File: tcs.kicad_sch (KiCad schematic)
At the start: 7 parts

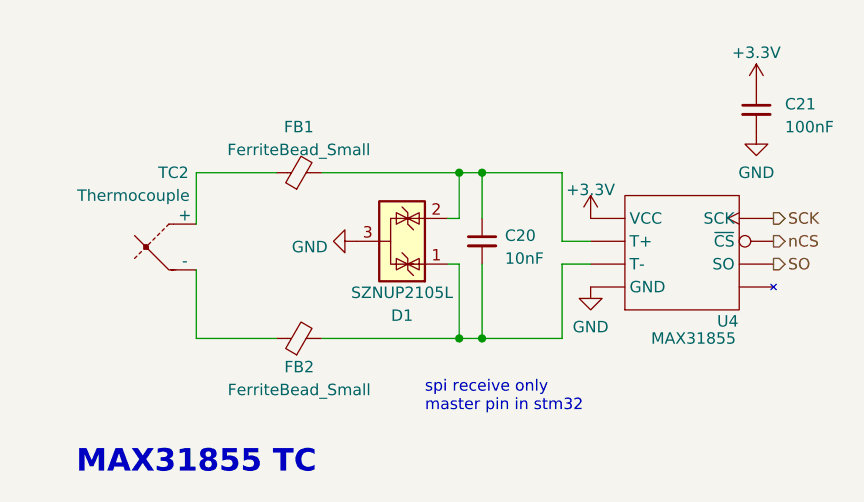
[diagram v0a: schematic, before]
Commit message: fixed resistor values
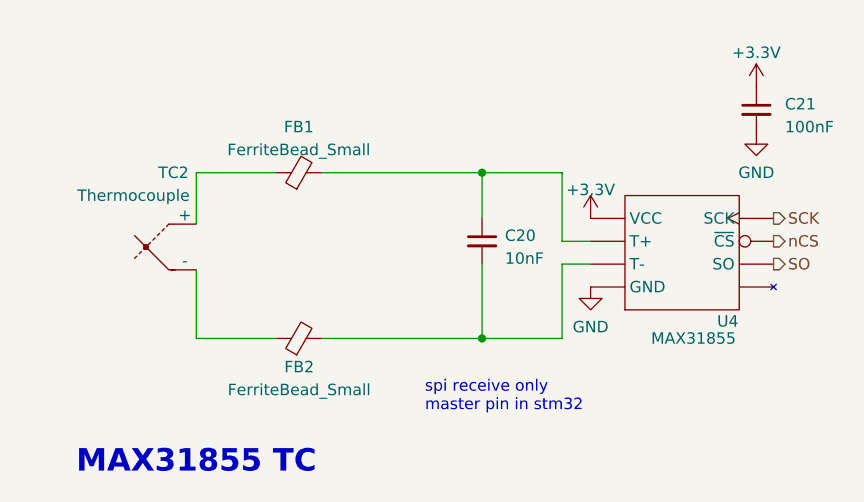
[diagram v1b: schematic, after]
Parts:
- removed D1: SZNUP2105L, Package_TO_SOT_SMD:SOT-23, symbol Power_Protection:SZNUP2105L
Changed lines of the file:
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@@
   (junction (at 143.51 92.075) (diameter 0) (color 0 0 0 0)
   )
-  (junction (at 140.97 73.66) (diameter 0) (color 0 0 0 0)
-  )
   (junction (at 143.51 73.66) (diameter 0) (color 0 0 0 0)
   )
-  (junction (at 140.97 92.075) (diameter 0) (color 0 0 0 0)
-  )
   (wire (pts (xy 111.76 79.375) (xy 111.76 73.66))
     (stroke (width 0) (type default))
@@
     (stroke (width 0) (type default))
   )
-  (wire (pts (xy 139.7 83.82) (xy 140.97 83.82))
-    (stroke (width 0) (type default))
-  )
   (wire (pts (xy 111.76 73.66) (xy 120.65 73.66))
     (stroke (width 0) (type default))
@@
     (stroke (width 0) (type default))
   )
-  (wire (pts (xy 140.97 78.74) (xy 139.7 78.74))
-    (stroke (width 0) (type default))
-  )
-  (wire (pts (xy 125.73 73.66) (xy 140.97 73.66))
+  (wire (pts (xy 125.73 73.66) (xy 143.51 73.66))
     (stroke (width 0) (type default))
   )
@@
     (stroke (width 0) (type default))
   )
-  (wire (pts (xy 125.73 92.075) (xy 140.97 92.075))
-    (stroke (width 0) (type default))
-  )
   (wire (pts (xy 143.51 92.075) (xy 152.4 92.075))
     (stroke (width 0) (type default))
   )
-  (wire (pts (xy 140.97 73.66) (xy 140.97 78.74))
-    (stroke (width 0) (type default))
-  )
-  (wire (pts (xy 140.97 83.82) (xy 140.97 92.075))
-    (stroke (width 0) (type default))
-  )
   (wire (pts (xy 143.51 73.66) (xy 152.4 73.66))
     (stroke (width 0) (type default))
   )
-  (wire (pts (xy 140.97 73.66) (xy 143.51 73.66))
-    (stroke (width 0) (type default))
-  )
   (wire (pts (xy 152.4 81.28) (xy 152.4 73.66))
     (stroke (width 0) (type default))
   )
-  (wire (pts (xy 140.97 92.075) (xy 143.51 92.075))
+  (wire (pts (xy 125.73 92.075) (xy 143.51 92.075))
     (stroke (width 0) (type default))
   )
@@
     )
   )
-  (symbol (lib_id "power:GND") (at 129.54 81.28 270) (unit 1)
-    (in_bom yes) (on_board yes) (dnp no) (fields_autoplaced)
-    (property "Reference" "#PWR013" (at 123.19 81.28 0)
-      (effects (font (size 1.27 1.27)) hide)
-    )
-    (property "Value" "GND" (at 126.365 81.915 90)
-      (effects (font (size 1.27 1.27)) (justify right))
-    )
-    (property "Footprint" "" (at 129.54 81.28 0)
-      (effects (font (size 1.27 1.27)) hide)
-    )
-    (property "Datasheet" "" (at 129.54 81.28 0)
-      (effects (font (size 1.27 1.27)) hide)
-    )
-    (pin "1")
-    (instances
-      (project "ECU_2.0_Proto1"
-        (path "/06e39eae-ccca-47c1-9146-3af0bb877e60"
-          (reference "#PWR013") (unit 1)
-        )
-      )
-      (project "TC_readings"
-        (path "/4e2048f0-e02d-4f9b-bba0-dfeebe43f4af"
-          (reference "#PWR01") (unit 1)
-        )
-      )
-      (project "TC_reading_2"
-        (path "/af2338e9-e09a-4a55-a9a1-2f1efd89145f"
-          (reference "#PWR01") (unit 1)
-        )
-      )
-      (project "rocket2-gse"
-        (path "/b7c1f72e-c0e1-45f4-a0c9-c80e8a0d5f55"
-          (reference "#PWR0182") (unit 1)
-        )
-      )
-      (project "rocket2-gse-hardware"
-        (path "/e56639b7-946f-4734-baa9-c73427e1cb23/9bfc3470-4af6-46f6-acbb-21e8d300e187"
-          (reference "#PWR0172") (unit 1)
-        )
-        (path "/e56639b7-946f-4734-baa9-c73427e1cb23/f72790a8-78c9-419b-8c68-ebc7218312f5"
-          (reference "#PWR0157") (unit 1)
-        )
-        (path "/e56639b7-946f-4734-baa9-c73427e1cb23/a2ab425d-6480-41eb-a8f0-de8cfd1045eb"
-          (reference "#PWR0152") (unit 1)
-        )
-        (path "/e56639b7-946f-4734-baa9-c73427e1cb23/e1e6b308-ee58-4d21-8c1c-f61b5a4bea2a"
-          (reference "#PWR0162") (unit 1)
-        )
-        (path "/e56639b7-946f-4734-baa9-c73427e1cb23/d4993af7-d6f7-454c-b0a9-d34995f1f991"
-          (reference "#PWR0167") (unit 1)
-        )
-        (path "/e56639b7-946f-4734-baa9-c73427e1cb23/6167aa15-868e-4467-9e6a-9a9cb675929f"
-          (reference "#PWR0147") (unit 1)
-        )
-      )
-    )
-  )
   (symbol (lib_id "power:GND") (at 155.575 86.36 0) (unit 1)
     (in_bom yes) (on_board yes) (dnp no) (fields_autoplaced)
@@
         )
       )
-    )
-  )
-  (symbol (lib_id "Power_Protection:SZNUP2105L") (at 134.62 81.28 270) (mirror x) (unit 1)
-    (in_bom yes) (on_board yes) (dnp no)
-    (property "Reference" "D1" (at 134.62 89.535 90)
-      (effects (font (size 1.27 1.27)))
-    )
-    (property "Value" "SZNUP2105L" (at 134.62 86.995 90)
-      (effects (font (size 1.27 1.27)))
-    )
-    (property "Footprint" "Package_TO_SOT_SMD:SOT-23" (at 133.35 75.565 0)
-      (effects (font (size 1.27 1.27)) (justify left) hide)
-    )
-    (property "Datasheet" "http://www.onsemi.com/pub_link/Collateral/NUP2105L-D.PDF" (at 137.795 78.105 0)
-      (effects (font (size 1.27 1.27)) hide)
-    )
-    (property "Manufacturer" "onsemi" (at 134.62 81.28 0)
-      (effects (font (size 1.27 1.27)) hide)
-    )
-    (property "Part #" "SZNUP2105L" (at 134.62 81.28 0)
-      (effects (font (size 1.27 1.27)) hide)
-    )
-    (pin "3")
-    (pin "1")
-    (pin "2")
-    (instances
-      (project "ECU_2.0_Proto1"
-        (path "/06e39eae-ccca-47c1-9146-3af0bb877e60"
-          (reference "D1") (unit 1)
-        )
-      )
-      (project "TC_readings"
-        (path "/4e2048f0-e02d-4f9b-bba0-dfeebe43f4af"
-          (reference "D1") (unit 1)
-        )
-      )
-      (project "TC_reading_2"
-        (path "/af2338e9-e09a-4a55-a9a1-2f1efd89145f"
-          (reference "D1") (unit 1)
-        )
-      )
-      (project "rocket2-gse"
-        (path "/b7c1f72e-c0e1-45f4-a0c9-c80e8a0d5f55"
-          (reference "D31") (unit 1)
-        )
-      )
-      (project "rocket2-gse-hardware"
-        (path "/e56639b7-946f-4734-baa9-c73427e1cb23/9bfc3470-4af6-46f6-acbb-21e8d300e187"
-          (reference "D32") (unit 1)
-        )
-        (path "/e56639b7-946f-4734-baa9-c73427e1cb23/f72790a8-78c9-419b-8c68-ebc7218312f5"
-          (reference "D29") (unit 1)
-        )
-        (path "/e56639b7-946f-4734-baa9-c73427e1cb23/a2ab425d-6480-41eb-a8f0-de8cfd1045eb"
-          (reference "D28") (unit 1)
-        )
-        (path "/e56639b7-946f-4734-baa9-c73427e1cb23/e1e6b308-ee58-4d21-8c1c-f61b5a4bea2a"
-          (reference "D30") (unit 1)
-        )
-        (path "/e56639b7-946f-4734-baa9-c73427e1cb23/d4993af7-d6f7-454c-b0a9-d34995f1f991"
-          (reference "D31") (unit 1)
-        )
-        (path "/e56639b7-946f-4734-baa9-c73427e1cb23/6167aa15-868e-4467-9e6a-9a9cb675929f"
-          (reference "D27") (unit 1)
-        )
-      )

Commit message: added full schematic and outdated pcb
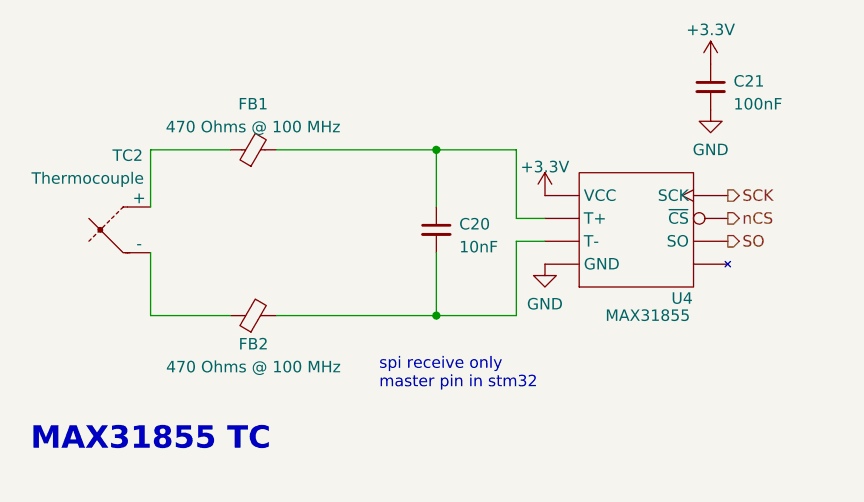
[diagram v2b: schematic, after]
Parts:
- C20, C21: symbol Device:C_Small -> UCIRP-KiCAD-Lib:C_Small
- FB1, FB2: value FerriteBead_Small -> 470 Ohms @ 100 MHz; symbol Device:FerriteBead_Small -> UCIRP-KiCAD-Lib:FerriteBead_Small
- TC2: footprint KiCad:AMKPCB -> UCIRP-KiCAD-Lib:AM-K-PCB; symbol Device:Thermocouple -> UCIRP-KiCAD-Lib:Thermocouple
- U4: symbol UCIRP-Symbols:MAX31855 -> UCIRP-KiCAD-Lib:MAX31855
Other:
- moved on the sheet: C20, C21, FB1, FB2, TC2, U4

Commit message: finished pcb design of gse 1.0
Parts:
- renumbered C21 to C?, C20 to C?, FB1 to FB?, FB2 to FB?, TC2 to TC?, U4 to U?
